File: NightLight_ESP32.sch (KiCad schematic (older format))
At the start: 24 parts, among them J1 USB_OTG, J2 BUTTON, Q1 MMBT2222, Q2 MMBT2222, SW1 TL3342, SW2 TL3342, U1 ESP32-WROOM-32D, U2 AP2112K-3.3, U3 CP2104

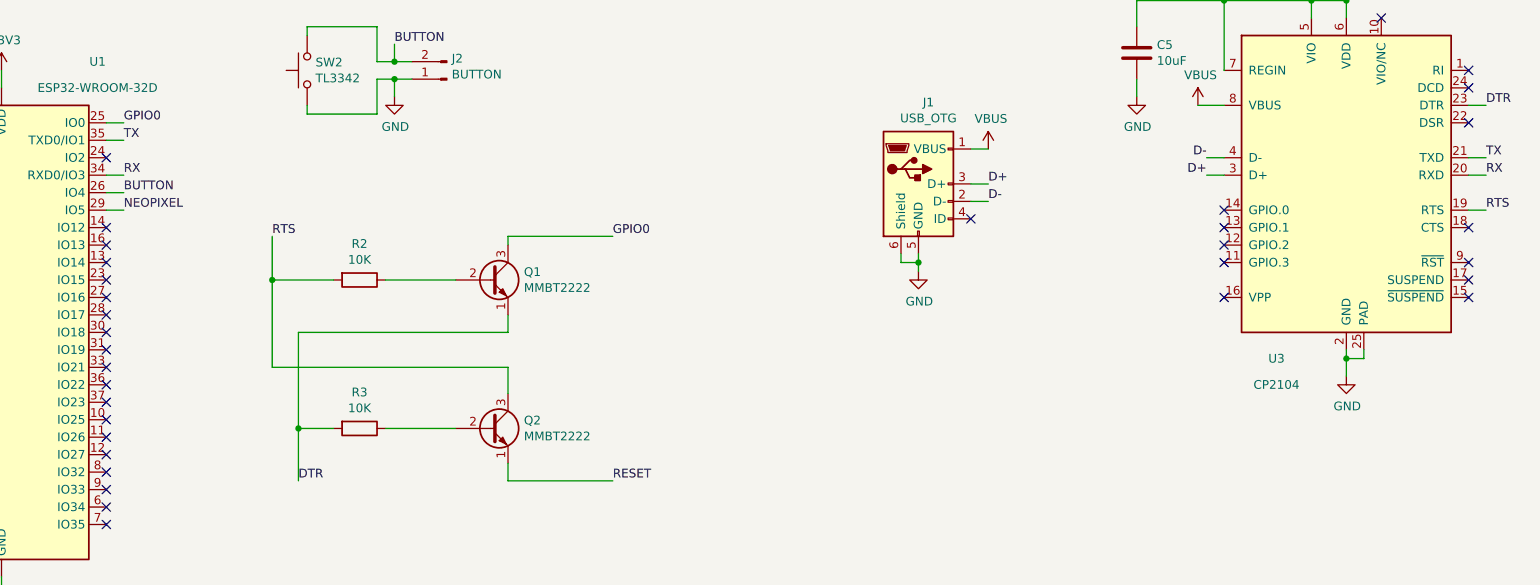
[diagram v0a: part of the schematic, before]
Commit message: Fixed issues with serial lines not being connected correctly
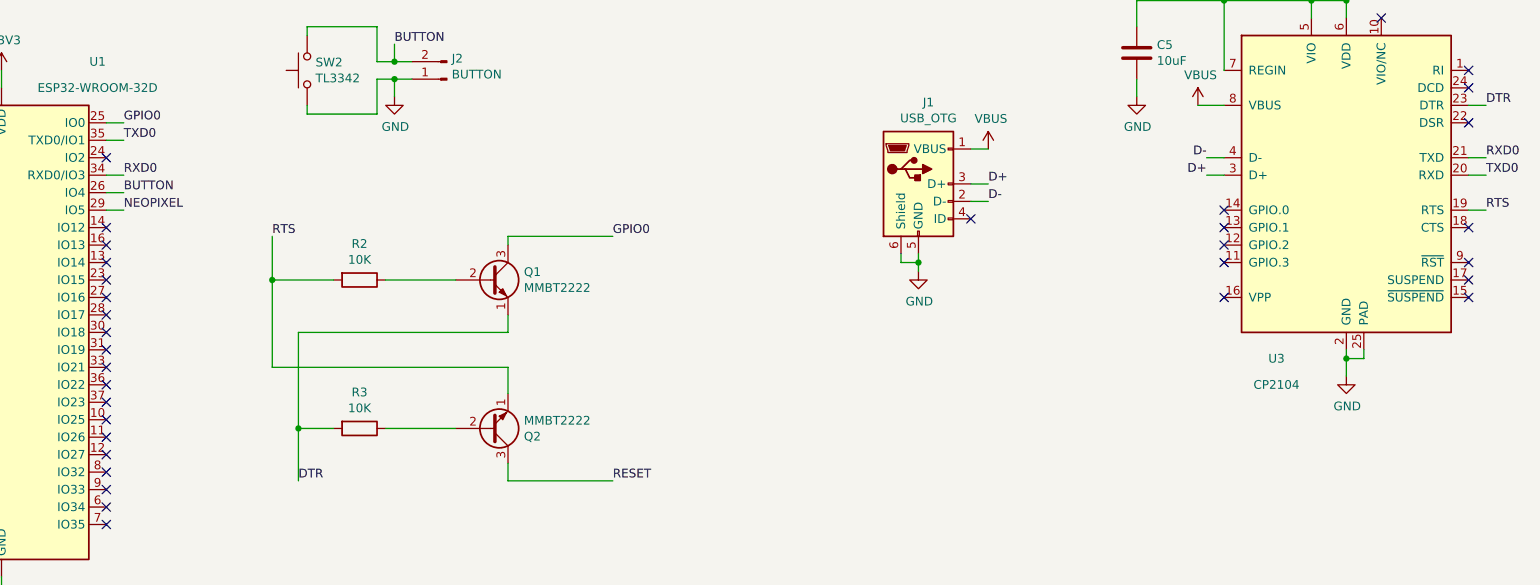
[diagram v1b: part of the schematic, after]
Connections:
- net RESET: now also Q2.3 (C); no longer Q2.1 (E)
- net RTS: now also Q2.1 (E); no longer Q2.3 (C)
- net RX renamed RXD0
- net RXD0: now also U3.21 (TXD); no longer U3.20 (RXD)
- net TX renamed TXD0
- net TXD0: now also U3.20 (RXD); no longer U3.21 (TXD)
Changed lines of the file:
@@
 F 3 "http://www.unisonic.com.tw/datasheet/S8050.pdf" H 4850 6400 50  0001 L CNN
 	1    4850 6400
-	1    0    0    -1
+	1    0    0    1
 $EndComp
 $Comp
@@
 GPIO0
 Text Label 2750 4750 0    50   ~ 0
-TX
+TXD0
 Text Label 2750 4950 0    50   ~ 0
-RX
+RXD0
 Wire Wire Line
 	2650 4750 2750 4750
@@
 $EndComp
 Text Label 10550 4850 0    50   ~ 0
-TX
+RXD0
 Text Label 10550 4950 0    50   ~ 0
-RX
+TXD0
 Wire Wire Line
 	10550 4950 10450 4950

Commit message: Updated LEDs power to be configurable from 5V or 3.3V
Should be ok with a small circuot like this but close to the limits
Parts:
- added JP1: SolderJumper_3_Bridged12, Jumper:SolderJumper-3_P1.3mm_Bridged12_RoundedPad1.0x1.5mm, symbol Jumper:SolderJumper_3_Bridged12
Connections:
- net +3V3: now also JP1.3 (B); no longer D1.1 (VDD), D2.1 (VDD), D3.1 (VDD), D4.1 (VDD), D5.1 (VDD), D6.1 (VDD)
- net VBUS: now also JP1.1 (A)
- new net LED_POWER: D1.1 (VDD), D2.1 (VDD), D3.1 (VDD), D4.1 (VDD), D5.1 (VDD), D6.1 (VDD), JP1.2 (C)
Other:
- moved on the sheet: D1, D2, D3, D4, D5, D6
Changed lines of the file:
@@
 L LED:WS2812B D1
 U 1 1 5F9F4DC2
-P 1650 2900
-F 0 "D1" H 1994 2946 50  0000 L CNN
-F 1 "WS2812B" H 1994 2855 50  0000 L CNN
-F 2 "LED_SMD:LED_WS2812B_PLCC4_5.0x5.0mm_P3.2mm" H 1700 2600 50  0001 L TNN
-F 3 "https://cdn-shop.adafruit.com/datasheets/WS2812B.pdf" H 1750 2525 50  0001 L TNN
-	1    1650 2900
+P 1600 3300
+F 0 "D1" H 1944 3346 50  0000 L CNN
+F 1 "WS2812B" H 1944 3255 50  0000 L CNN
+F 2 "LED_SMD:LED_WS2812B_PLCC4_5.0x5.0mm_P3.2mm" H 1650 3000 50  0001 L TNN
+F 3 "https://cdn-shop.adafruit.com/datasheets/WS2812B.pdf" H 1700 2925 50  0001 L TNN
+	1    1600 3300
 	1    0    0    -1
 $EndComp
@@
 L LED:WS2812B D2
 U 1 1 5F9F5C9D
-P 2600 2900
-F 0 "D2" H 2944 2946 50  0000 L CNN
-F 1 "WS2812B" H 2944 2855 50  0000 L CNN
-F 2 "LED_SMD:LED_WS2812B_PLCC4_5.0x5.0mm_P3.2mm" H 2650 2600 50  0001 L TNN
-F 3 "https://cdn-shop.adafruit.com/datasheets/WS2812B.pdf" H 2700 2525 50  0001 L TNN
-	1    2600 2900
+P 2550 3300
+F 0 "D2" H 2894 3346 50  0000 L CNN
+F 1 "WS2812B" H 2894 3255 50  0000 L CNN
+F 2 "LED_SMD:LED_WS2812B_PLCC4_5.0x5.0mm_P3.2mm" H 2600 3000 50  0001 L TNN
+F 3 "https://cdn-shop.adafruit.com/datasheets/WS2812B.pdf" H 2650 2925 50  0001 L TNN
+	1    2550 3300
 	1    0    0    -1
 $EndComp
@@
 L LED:WS2812B D3
 U 1 1 5F9F6440
-P 3550 2900
-F 0 "D3" H 3894 2946 50  0000 L CNN
-F 1 "WS2812B" H 3894 2855 50  0000 L CNN
-F 2 "LED_SMD:LED_WS2812B_PLCC4_5.0x5.0mm_P3.2mm" H 3600 2600 50  0001 L TNN
-F 3 "https://cdn-shop.adafruit.com/datasheets/WS2812B.pdf" H 3650 2525 50  0001 L TNN
-	1    3550 2900
+P 3500 3300
+F 0 "D3" H 3844 3346 50  0000 L CNN
+F 1 "WS2812B" H 3844 3255 50  0000 L CNN
+F 2 "LED_SMD:LED_WS2812B_PLCC4_5.0x5.0mm_P3.2mm" H 3550 3000 50  0001 L TNN
+F 3 "https://cdn-shop.adafruit.com/datasheets/WS2812B.pdf" H 3600 2925 50  0001 L TNN
+	1    3500 3300
 	1    0    0    -1
 $EndComp
@@
 L LED:WS2812B D4
 U 1 1 5F9F6CD7
-P 4500 2900
-F 0 "D4" H 4844 2946 50  0000 L CNN
-F 1 "WS2812B" H 4844 2855 50  0000 L CNN
-F 2 "LED_SMD:LED_WS2812B_PLCC4_5.0x5.0mm_P3.2mm" H 4550 2600 50  0001 L TNN
-F 3 "https://cdn-shop.adafruit.com/datasheets/WS2812B.pdf" H 4600 2525 50  0001 L TNN
-	1    4500 2900
+P 4450 3300
+F 0 "D4" H 4794 3346 50  0000 L CNN
+F 1 "WS2812B" H 4794 3255 50  0000 L CNN
+F 2 "LED_SMD:LED_WS2812B_PLCC4_5.0x5.0mm_P3.2mm" H 4500 3000 50  0001 L TNN
+F 3 "https://cdn-shop.adafruit.com/datasheets/WS2812B.pdf" H 4550 2925 50  0001 L TNN
+	1    4450 3300
 	1    0    0    -1
 $EndComp
@@
 Wire Wire Line
 	2050 7350 2050 7250
-Text Label 1250 2900 2    50   ~ 0
+Text Label 1200 3300 2    50   ~ 0
 NEOPIXEL
 Wire Wire Line
-	1250 2900 1350 2900
+	1200 3300 1300 3300
 Text Label 2750 5150 0    50   ~ 0
 NEOPIXEL
@@
 	2650 5150 2750 5150
 Wire Wire Line
-	1650 2600 1650 2500
-Wire Wire Line
-	1650 2500 2600 2500
-Wire Wire Line
-	2600 2500 2600 2600
-Wire Wire Line
-	2600 2500 3100 2500
-Wire Wire Line
-	3550 2500 3550 2600
-Connection ~ 2600 2500
-Wire Wire Line
-	3550 2500 4500 2500
-Wire Wire Line
-	4500 2500 4500 2600
-Connection ~ 3550 2500
-Wire Wire Line
-	3100 2500 3100 2400
-Connection ~ 3100 2500
-Wire Wire Line
-	3100 2500 3550 2500
-Wire Wire Line
-	1650 3200 1650 3300
-Wire Wire Line
-	1650 3300 2600 3300
-Wire Wire Line
-	2600 3300 2600 3200
-Wire Wire Line
-	2600 3300 3100 3300
-Wire Wire Line
-	3550 3300 3550 3200
-Connection ~ 2600 3300
-Wire Wire Line
-	3550 3300 4500 3300
-Wire Wire Line
-	4500 3300 4500 3200
-Connection ~ 3550 3300
-Wire Wire Line
-	1950 2900 2300 2900
-Wire Wire Line
-	2900 2900 3250 2900
-Wire Wire Line
-	3850 2900 4200 2900
-Wire Wire Line
-	3100 3300 3100 3400
-Connection ~ 3100 3300
-Wire Wire Line
-	3100 3300 3550 3300
+	1600 3000 1600 2900
+Wire Wire Line
+	1600 2900 2550 2900
+Wire Wire Line
+	2550 2900 2550 3000
+Wire Wire Line
+	3500 2900 3500 3000
+Connection ~ 2550 2900
+Wire Wire Line
+	3500 2900 4000 2900
+Wire Wire Line
+	4450 2900 4450 3000
+Connection ~ 3500 2900
+Wire Wire Line
+	7450 1700 7450 1600
+Wire Wire Line
+	1600 3600 1600 3700
+Wire Wire Line
+	1600 3700 2550 3700
+Wire Wire Line
+	2550 3700 2550 3600
+Wire Wire Line
+	2550 3700 3050 3700
+Wire Wire Line
+	3500 3700 3500 3600
+Connection ~ 2550 3700
+Wire Wire Line
+	3500 3700 4450 3700
+Wire Wire Line
+	4450 3700 4450 3600
+Connection ~ 3500 3700
+Wire Wire Line
+	1900 3300 2250 3300
+Wire Wire Line
+	2850 3300 3200 3300
+Wire Wire Line
+	3800 3300 4150 3300
+Wire Wire Line
+	3050 3700 3050 3800
+Connection ~ 3050 3700
+Wire Wire Line
+	3050 3700 3500 3700
 $Comp
 L power:GND #PWR0113
 U 1 1 5FA10661
-P 3100 3400
-F 0 "#PWR0113" H 3100 3150 50  0001 C CNN
-F 1 "GND" H 3105 3227 50  0000 C CNN
-F 2 "" H 3100 3400 50  0001 C CNN
-F 3 "" H 3100 3400 50  0001 C CNN
-	1    3100 3400
-	1    0    0    -1
-$EndComp
-$Comp
-L power:+3V3 #PWR0114
-U 1 1 5FA10A71
-P 3100 2400
-F 0 "#PWR0114" H 3100 2250 50  0001 C CNN
-F 1 "+3V3" H 3115 2573 50  0000 C CNN
-F 2 "" H 3100 2400 50  0001 C CNN
-F 3 "" H 3100 2400 50  0001 C CNN
-	1    3100 2400
+P 3050 3800
+F 0 "#PWR0113" H 3050 3550 50  0001 C CNN
+F 1 "GND" H 3055 3627 50  0000 C CNN
+F 2 "" H 3050 3800 50  0001 C CNN
+F 3 "" H 3050 3800 50  0001 C CNN
+	1    3050 3800
 	1    0    0    -1
 $EndComp
@@
 L LED:WS2812B D5
 U 1 1 5FBCF5A5
-P 5450 2900
-F 0 "D5" H 5794 2946 50  0000 L CNN
-F 1 "WS2812B" H 5794 2855 50  0000 L CNN
-F 2 "LED_SMD:LED_WS2812B_PLCC4_5.0x5.0mm_P3.2mm" H 5500 2600 50  0001 L TNN
-F 3 "https://cdn-shop.adafruit.com/datasheets/WS2812B.pdf" H 5550 2525 50  0001 L TNN
-	1    5450 2900
+P 5400 3300
+F 0 "D5" H 5744 3346 50  0000 L CNN
+F 1 "WS2812B" H 5744 3255 50  0000 L CNN
+F 2 "LED_SMD:LED_WS2812B_PLCC4_5.0x5.0mm_P3.2mm" H 5450 3000 50  0001 L TNN
+F 3 "https://cdn-shop.adafruit.com/datasheets/WS2812B.pdf" H 5500 2925 50  0001 L TNN
+	1    5400 3300
 	1    0    0    -1
 $EndComp
@@
 L LED:WS2812B D6
 U 1 1 5FBD0096
-P 6400 2900
-F 0 "D6" H 6744 2946 50  0000 L CNN
-F 1 "WS2812B" H 6744 2855 50  0000 L CNN
-F 2 "LED_SMD:LED_WS2812B_PLCC4_5.0x5.0mm_P3.2mm" H 6450 2600 50  0001 L TNN
-F 3 "https://cdn-shop.adafruit.com/datasheets/WS2812B.pdf" H 6500 2525 50  0001 L TNN
-	1    6400 2900
-	1    0    0    -1
-$EndComp
-Wire Wire Line
-	4800 2900 5150 2900
-Wire Wire Line
-	5750 2900 6100 2900
-NoConn ~ 6700 2900
-Wire Wire Line
-	6400 2600 6400 2500
-Wire Wire Line
-	6400 2500 5450 2500
-Connection ~ 4500 2500
-Wire Wire Line
-	4500 3300 5450 3300
-Wire Wire Line
-	6400 3300 6400 3200
-Connection ~ 4500 3300
-Wire Wire Line
-	5450 3200 5450 3300
-Connection ~ 5450 3300
-Wire Wire Line
-	5450 3300 6400 3300
-Wire Wire Line
-	5450 2600 5450 2500
-Connection ~ 5450 2500
-Wire Wire Line
-	5450 2500 4500 2500
+P 6350 3300
+F 0 "D6" H 6694 3346 50  0000 L CNN
+F 1 "WS2812B" H 6694 3255 50  0000 L CNN
+F 2 "LED_SMD:LED_WS2812B_PLCC4_5.0x5.0mm_P3.2mm" H 6400 3000 50  0001 L TNN
+F 3 "https://cdn-shop.adafruit.com/datasheets/WS2812B.pdf" H 6450 2925 50  0001 L TNN
+	1    6350 3300
+	1    0    0    -1
+$EndComp
+Wire Wire Line
+	4750 3300 5100 3300
+Wire Wire Line
+	5700 3300 6050 3300
+NoConn ~ 6650 3300
+Wire Wire Line
+	6350 3000 6350 2900
+Wire Wire Line
+	6350 2900 5400 2900
+Connection ~ 4450 2900
+Wire Wire Line
+	4450 3700 5400 3700
+Wire Wire Line
+	6350 3700 6350 3600
+Connection ~ 4450 3700
+Wire Wire Line
+	5400 3600 5400 3700
+Connection ~ 5400 3700
+Wire Wire Line
+	5400 3700 6350 3700
+Wire Wire Line
+	5400 3000 5400 2900
+Connection ~ 5400 2900
+Wire Wire Line
+	5400 2900 4450 2900
+$Comp
+L power:VBUS #PWR0114
+U 1 1 60170019
+P 6850 1350
+F 0 "#PWR0114" H 6850 1200 50  0001 C CNN
+F 1 "VBUS" H 6865 1523 50  0000 C CNN
+F 2 "" H 6850 1350 50  0001 C CNN
+F 3 "" H 6850 1350 50  0001 C CNN
+	1    6850 1350
+	1    0    0    -1
+$EndComp
+$Comp
+L Jumper:SolderJumper_3_Bridged12 JP1
+U 1 1 6025AF24
+P 7450 1450
+F 0 "JP1" H 7450 1655 50  0000 C CNN
+F 1 "SolderJumper_3_Bridged12" H 7450 1564 50  0000 C CNN
+F 2 "Jumper:SolderJumper-3_P1.3mm_Bridged12_RoundedPad1.0x1.5mm" H 7450 1450 50  0001 C CNN
+F 3 "~" H 7450 1450 50  0001 C CNN
+	1    7450 1450
+	1    0    0    -1
+$EndComp
+Wire Wire Line
+	6850 1350 6850 1450
+Wire Wire Line
+	6850 1450 7250 1450
+Wire Wire Line
+	7650 1450 8050 1450
+Wire Wire Line
+	8050 1450 8050 1350
+Wire Wire Line
+	2550 2900 3500 2900
+Text Label 4000 2700 0    50   ~ 0
+LED_POWER
+Wire Wire Line
+	4000 2700 4000 2900
+Connection ~ 4000 2900
+Wire Wire Line
+	4000 2900 4450 2900
+Text Label 7450 1700 0    50   ~ 0
+LED_POWER
+$Comp
+L power:+3V3 #PWR01
+U 1 1 602A7389
+P 8050 1350
+F 0 "#PWR01" H 8050 1200 50  0001 C CNN
+F 1 "+3V3" H 8065 1523 50  0000 C CNN
+F 2 "" H 8050 1350 50  0001 C CNN
+F 3 "" H 8050 1350 50  0001 C CNN
+	1    8050 1350
+	1    0    0    -1
+$EndComp
+$Comp
+L power:PWR_FLAG #FLG01
+U 1 1 602AC6E8
+P 750 1050
+F 0 "#FLG01" H 750 1125 50  0001 C CNN
+F 1 "PWR_FLAG" H 750 1223 50  0000 C CNN
+F 2 "" H 750 1050 50  0001 C CNN
+F 3 "~" H 750 1050 50  0001 C CNN
+	1    750  1050
+	-1   0    0    1
+$EndComp
+Text Label 750  950  1    50   ~ 0
+LED_POWER
+Wire Wire Line
+	750  950  750  1050
 $EndSCHEMATC

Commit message: Changed to KiKit to generate the fabrication files
including JLCPCB part numbers and position fixes
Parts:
- C1, C2, C3, C5: LCSC (none) -> C15850
- C4: LCSC (none) -> C28323
- D1, D2, D3, D4, D5, D6: JLCPCB_CORRECTION (none) -> 0;0;180; LCSC (none) -> C114586
- J1: LCSC (none) -> C21377
- Q1, Q2: JLCPCB_CORRECTION (none) -> 0;0;180; LCSC (none) -> C181121
- R1: LCSC (none) -> C17407
- R2, R3, R4: LCSC (none) -> C17414
- SW1, SW2: LCSC (none) -> C318884
- U1: JLCPCB_CORRECTION (none) -> 0;-3;270; LCSC (none) -> C473012
- U2: LCSC (none) -> C51118
- U3: LCSC (none) -> C47742
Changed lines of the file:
@@
 F 2 "RF_Module:ESP32-WROOM-32" H 2050 4350 50  0001 C CNN
 F 3 "https://www.espressif.com/sites/default/files/documentation/esp32-wroom-32d_esp32-wroom-32u_datasheet_en.pdf" H 1750 5900 50  0001 C CNN
+F 4 "C473012" H 2050 5850 50  0001 C CNN "LCSC"
+F 5 "0;-3;270" H 2050 5850 50  0001 C CNN "JLCPCB_CORRECTION"
 	1    2050 5850
 	1    0    0    -1
@@
 F 2 "Package_DFN_QFN:QFN-24-1EP_4x4mm_P0.5mm_EP2.6x2.6mm" H 9900 4000 50  0001 L CNN
 F 3 "https://www.silabs.com/documents/public/data-sheets/cp2104.pdf" H 9200 6200 50  0001 C CNN
+F 4 "C47742" H 9750 4950 50  0001 C CNN "LCSC"
 	1    9750 4950
 	1    0    0    -1
@@
 F 2 "Connector_USB:USB_Micro-B_Amphenol_10103594-0001LF_Horizontal" H 7450 4950 50  0001 C CNN
 F 3 " ~" H 7450 4950 50  0001 C CNN
+F 4 "C21377" H 7300 5000 50  0001 C CNN "LCSC"
 	1    7300 5000
 	1    0    0    -1
@@
 F 2 "Resistor_SMD:R_0805_2012Metric" V 4880 1150 50  0001 C CNN
 F 3 "~" H 4950 1150 50  0001 C CNN
+F 4 "C17414" H 4950 1150 50  0001 C CNN "LCSC"
 	1    4950 1150
 	1    0    0    -1
@@
 F 2 "Button_Switch_SMD:SW_SPST_TL3342" H 4950 1800 50  0001 C CNN
 F 3 "~" H 4950 1800 50  0001 C CNN
+F 4 "C318884" H 4950 1600 50  0001 C CNN "LCSC"
 	1    4950 1600
 	0    -1   -1   0
@@
 F 2 "Capacitor_SMD:C_0805_2012Metric" H 5588 1450 50  0001 C CNN
 F 3 "~" H 5550 1600 50  0001 C CNN
+F 4 "C28323" H 5550 1600 50  0001 C CNN "LCSC"
 	1    5550 1600
 	-1   0    0    1
@@
 F 2 "Capacitor_SMD:C_0805_2012Metric" H 4138 1350 50  0001 C CNN
 F 3 "~" H 4100 1500 50  0001 C CNN
+F 4 "C15850" H 4100 1500 50  0001 C CNN "LCSC"
 	1    4100 1500
 	1    0    0    -1
@@
 F 2 "Package_TO_SOT_SMD:SOT-23-5" H 2750 1675 50  0001 C CNN
 F 3 "https://www.diodes.com/assets/Datasheets/AP2112.pdf" H 2750 1450 50  0001 C CNN
+F 4 "C51118" H 2750 1350 50  0001 C CNN "LCSC"
 	1    2750 1350
 	1    0    0    -1
@@
 F 2 "Resistor_SMD:R_0805_2012Metric" V 2180 1500 50  0001 C CNN
 F 3 "~" H 2250 1500 50  0001 C CNN
+F 4 "C17407" H 2250 1500 50  0001 C CNN "LCSC"
 	1    2250 1500
 	1    0    0    -1
@@
 F 2 "Capacitor_SMD:C_0805_2012Metric" H 3538 1350 50  0001 C CNN
 F 3 "~" H 3500 1500 50  0001 C CNN
+F 4 "C15850" H 3500 1500 50  0001 C CNN "LCSC"
 	1    3500 1500
 	1    0    0    -1
@@
 F 2 "Capacitor_SMD:C_0805_2012Metric" H 1838 1350 50  0001 C CNN
 F 3 "~" H 1800 1500 50  0001 C CNN
+F 4 "C15850" H 1800 1500 50  0001 C CNN "LCSC"
 	1    1800 1500
 	1    0    0    -1
@@
 F 2 "LED_SMD:LED_WS2812B_PLCC4_5.0x5.0mm_P3.2mm" H 1650 3000 50  0001 L TNN
 F 3 "https://cdn-shop.adafruit.com/datasheets/WS2812B.pdf" H 1700 2925 50  0001 L TNN
+F 4 "C114586" H 1600 3300 50  0001 C CNN "LCSC"
+F 5 "0;0;180" H 1600 3300 50  0001 C CNN "JLCPCB_CORRECTION"
 	1    1600 3300
 	1    0    0    -1
@@
 F 2 "LED_SMD:LED_WS2812B_PLCC4_5.0x5.0mm_P3.2mm" H 2600 3000 50  0001 L TNN
 F 3 "https://cdn-shop.adafruit.com/datasheets/WS2812B.pdf" H 2650 2925 50  0001 L TNN
+F 4 "0;0;180" H 2550 3300 50  0001 C CNN "JLCPCB_CORRECTION"
+F 5 "C114586" H 2550 3300 50  0001 C CNN "LCSC"
 	1    2550 3300
 	1    0    0    -1
@@
 F 2 "LED_SMD:LED_WS2812B_PLCC4_5.0x5.0mm_P3.2mm" H 3550 3000 50  0001 L TNN
 F 3 "https://cdn-shop.adafruit.com/datasheets/WS2812B.pdf" H 3600 2925 50  0001 L TNN
+F 4 "0;0;180" H 3500 3300 50  0001 C CNN "JLCPCB_CORRECTION"
+F 5 "C114586" H 3500 3300 50  0001 C CNN "LCSC"
 	1    3500 3300
 	1    0    0    -1
@@
 F 2 "LED_SMD:LED_WS2812B_PLCC4_5.0x5.0mm_P3.2mm" H 4500 3000 50  0001 L TNN
 F 3 "https://cdn-shop.adafruit.com/datasheets/WS2812B.pdf" H 4550 2925 50  0001 L TNN
+F 4 "0;0;180" H 4450 3300 50  0001 C CNN "JLCPCB_CORRECTION"
+F 5 "C114586" H 4450 3300 50  0001 C CNN "LCSC"
 	1    4450 3300
 	1    0    0    -1
@@
 F 2 "Package_TO_SOT_SMD:SOT-23" H 5050 5475 50  0001 L CIN
 F 3 "http://www.unisonic.com.tw/datasheet/S8050.pdf" H 4850 5550 50  0001 L CNN
+F 4 "C181121" H 4850 5550 50  0001 C CNN "LCSC"
+F 5 "0;0;180" H 4850 5550 50  0001 C CNN "JLCPCB_CORRECTION"
 	1    4850 5550
 	1    0    0    -1
@@
 F 2 "Package_TO_SOT_SMD:SOT-23" H 5050 6325 50  0001 L CIN
 F 3 "http://www.unisonic.com.tw/datasheet/S8050.pdf" H 4850 6400 50  0001 L CNN
+F 4 "C181121" H 4850 6400 50  0001 C CNN "LCSC"
+F 5 "0;0;180" H 4850 6400 50  0001 C CNN "JLCPCB_CORRECTION"
 	1    4850 6400
 	1    0    0    1
@@
 F 2 "Resistor_SMD:R_0805_2012Metric" V 4030 5550 50  0001 C CNN
 F 3 "~" H 4100 5550 50  0001 C CNN
+F 4 "C17414" H 4100 5550 50  0001 C CNN "LCSC"
 	1    4100 5550
 	0    1    1    0
@@
 F 2 "Resistor_SMD:R_0805_2012Metric" V 4030 6400 50  0001 C CNN
 F 3 "~" H 4100 6400 50  0001 C CNN
+F 4 "C17414" H 4100 6400 50  0001 C CNN "LCSC"
 	1    4100 6400
 	0    1    1    0
@@
 F 2 "Capacitor_SMD:C_0805_2012Metric" H 8588 4100 50  0001 C CNN
 F 3 "~" H 8550 4250 50  0001 C CNN
+F 4 "C15850" H 8550 4250 50  0001 C CNN "LCSC"
 	1    8550 4250
 	1    0    0    -1
@@
 F 2 "Button_Switch_SMD:SW_SPST_TL3342" H 3800 4550 50  0001 C CNN
 F 3 "~" H 3800 4550 50  0001 C CNN
+F 4 "C318884" H 3800 4350 50  0001 C CNN "LCSC"
 	1    3800 4350
 	0    -1   -1   0
@@
 F 2 "LED_SMD:LED_WS2812B_PLCC4_5.0x5.0mm_P3.2mm" H 5450 3000 50  0001 L TNN
 F 3 "https://cdn-shop.adafruit.com/datasheets/WS2812B.pdf" H 5500 2925 50  0001 L TNN
+F 4 "0;0;180" H 5400 3300 50  0001 C CNN "JLCPCB_CORRECTION"
+F 5 "C114586" H 5400 3300 50  0001 C CNN "LCSC"
 	1    5400 3300
 	1    0    0    -1
@@
 F 2 "LED_SMD:LED_WS2812B_PLCC4_5.0x5.0mm_P3.2mm" H 6400 3000 50  0001 L TNN
 F 3 "https://cdn-shop.adafruit.com/datasheets/WS2812B.pdf" H 6450 2925 50  0001 L TNN
+F 4 "0;0;180" H 6350 3300 50  0001 C CNN "JLCPCB_CORRECTION"
+F 5 "C114586" H 6350 3300 50  0001 C CNN "LCSC"
 	1    6350 3300
 	1    0    0    -1
